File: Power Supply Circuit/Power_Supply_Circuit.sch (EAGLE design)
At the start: 12 parts, among them U1 AP65111AWU-7

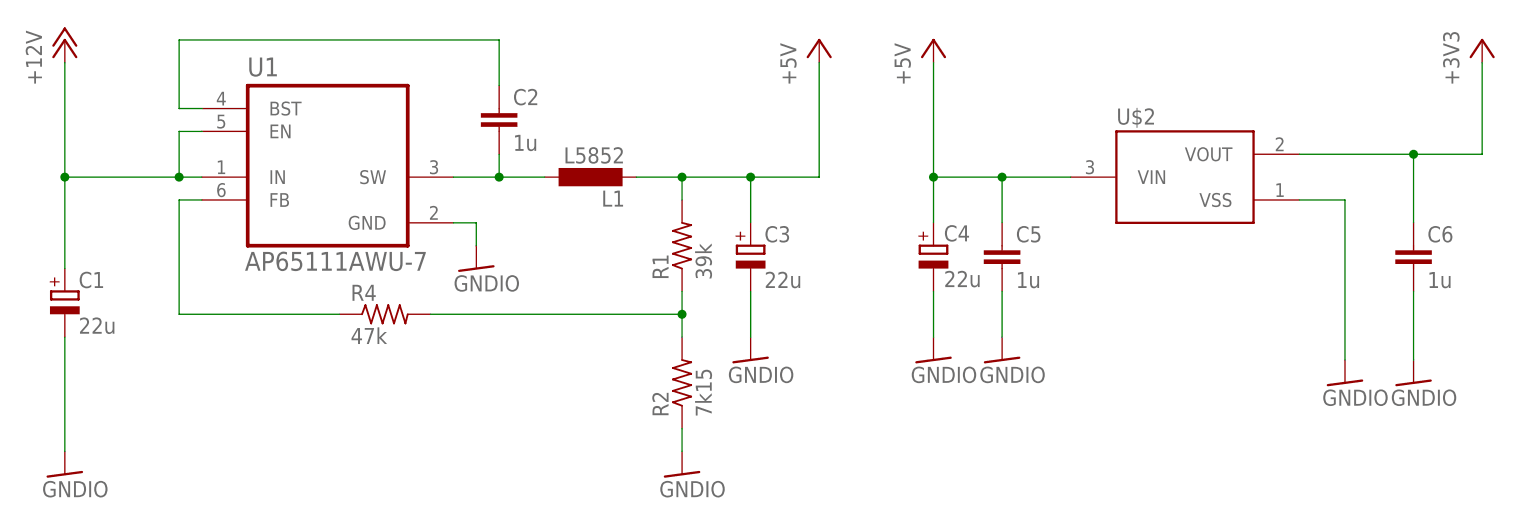
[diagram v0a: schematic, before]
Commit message: 電源周りの回路の修正
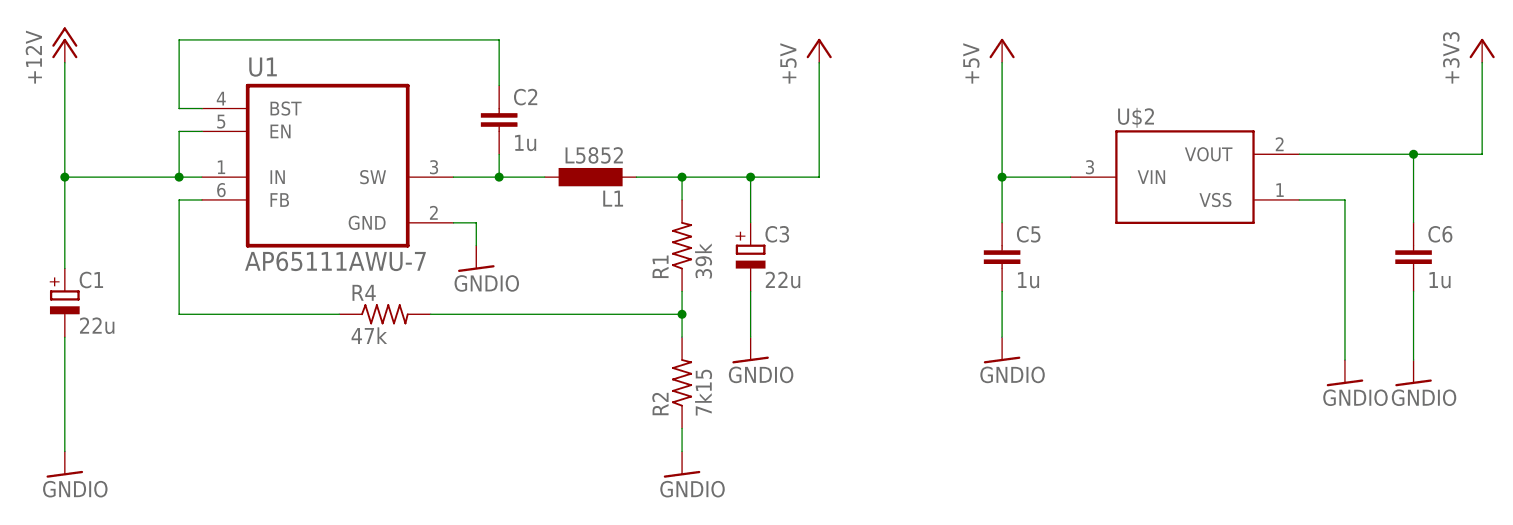
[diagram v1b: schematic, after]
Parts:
- removed C4: 22u, rcl:CPOL-EUE3.5-8
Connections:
- net +5V: no longer C4.+
- net GNDIO: no longer C4.-
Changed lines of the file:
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@@
 <?xml version="1.0" encoding="utf-8"?>
 <!DOCTYPE eagle SYSTEM "eagle.dtd">
-<eagle version="9.3.2">
+<eagle version="9.4.2">
 <drawing>
 <settings>
@@
 <part name="U$2" library="torex" deviceset="AP2120" device="" package3d_urn="urn:adsk.eagle:package:6993131/1"/>
 <part name="P+3" library="supply1" library_urn="urn:adsk.eagle:library:371" deviceset="+5V" device=""/>
-<part name="C4" library="rcl" library_urn="urn:adsk.eagle:library:334" deviceset="CPOL-EU" device="E3.5-8" package3d_urn="urn:adsk.eagle:package:23360/2" value="22u"/>
 <part name="C5" library="rcl" library_urn="urn:adsk.eagle:library:334" deviceset="C-EU" device="C0603" package3d_urn="urn:adsk.eagle:package:23616/2" value="1u"/>
 <part name="C6" library="rcl" library_urn="urn:adsk.eagle:library:334" deviceset="C-EU" device="C0603" package3d_urn="urn:adsk.eagle:package:23616/2" value="1u"/>
-<part name="GND5" library="supply1" library_urn="urn:adsk.eagle:library:371" deviceset="GNDIO" device=""/>
 <part name="GND6" library="supply1" library_urn="urn:adsk.eagle:library:371" deviceset="GNDIO" device=""/>
 <part name="GND7" library="supply1" library_urn="urn:adsk.eagle:library:371" deviceset="GNDIO" device=""/>
@@
 <attribute name="NAME" x="119.38" y="73.66" size="1.778" layer="95" rot="MR180"/>
 </instance>
-<instance part="P+3" gate="1" x="99.06" y="81.28" smashed="yes">
-<attribute name="VALUE" x="96.52" y="76.2" size="1.778" layer="96" rot="R90"/>
-</instance>
-<instance part="C4" gate="G$1" x="99.06" y="58.42" smashed="yes">
-<attribute name="NAME" x="100.203" y="58.9026" size="1.778" layer="95"/>
-<attribute name="VALUE" x="100.203" y="53.8226" size="1.778" layer="96"/>
+<instance part="P+3" gate="1" x="106.68" y="81.28" smashed="yes">
+<attribute name="VALUE" x="104.14" y="76.2" size="1.778" layer="96" rot="R90"/>
 </instance>
 <instance part="C5" gate="G$1" x="106.68" y="58.42" smashed="yes">
@@
 <attribute name="NAME" x="153.924" y="58.801" size="1.778" layer="95"/>
 <attribute name="VALUE" x="153.924" y="53.721" size="1.778" layer="96"/>
-</instance>
-<instance part="GND5" gate="G$1" x="99.06" y="45.72" smashed="yes">
-<attribute name="VALUE" x="96.52" y="43.18" size="1.778" layer="96"/>
 </instance>
 <instance part="GND6" gate="G$1" x="106.68" y="45.72" smashed="yes">
@@
 </segment>
 <segment>
-<pinref part="C4" gate="G$1" pin="-"/>
-<pinref part="GND5" gate="G$1" pin="GNDIO"/>
-<wire x1="99.06" y1="48.26" x2="99.06" y2="53.34" width="0.1524" layer="91"/>
-</segment>
-<segment>
 <pinref part="C5" gate="G$1" pin="2"/>
 <pinref part="GND6" gate="G$1" pin="GNDIO"/>
@@
 <segment>
 <pinref part="P+3" gate="1" pin="+5V"/>
-<wire x1="99.06" y1="60.96" x2="99.06" y2="66.04" width="0.1524" layer="91"/>
-<pinref part="C4" gate="G$1" pin="+"/>
 <pinref part="U$2" gate="G$1" pin="VIN"/>
-<wire x1="99.06" y1="66.04" x2="99.06" y2="78.74" width="0.1524" layer="91"/>
+<wire x1="106.68" y1="66.04" x2="106.68" y2="78.74" width="0.1524" layer="91"/>
 <wire x1="114.3" y1="66.04" x2="106.68" y2="66.04" width="0.1524" layer="91"/>
-<junction x="99.06" y="66.04"/>
 <pinref part="C5" gate="G$1" pin="1"/>
-<wire x1="106.68" y1="66.04" x2="99.06" y2="66.04" width="0.1524" layer="91"/>
 <wire x1="106.68" y1="60.96" x2="106.68" y2="66.04" width="0.1524" layer="91"/>
 <junction x="106.68" y="66.04"/>
